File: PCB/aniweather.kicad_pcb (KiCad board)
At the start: 2 copper layers, 55 x 75 mm, 36 parts, among them SW2 SW_Push, SW3 SW_Push, SW4 SW_DIP_x01, U4 TPS2116DRL, U5 TPS63001

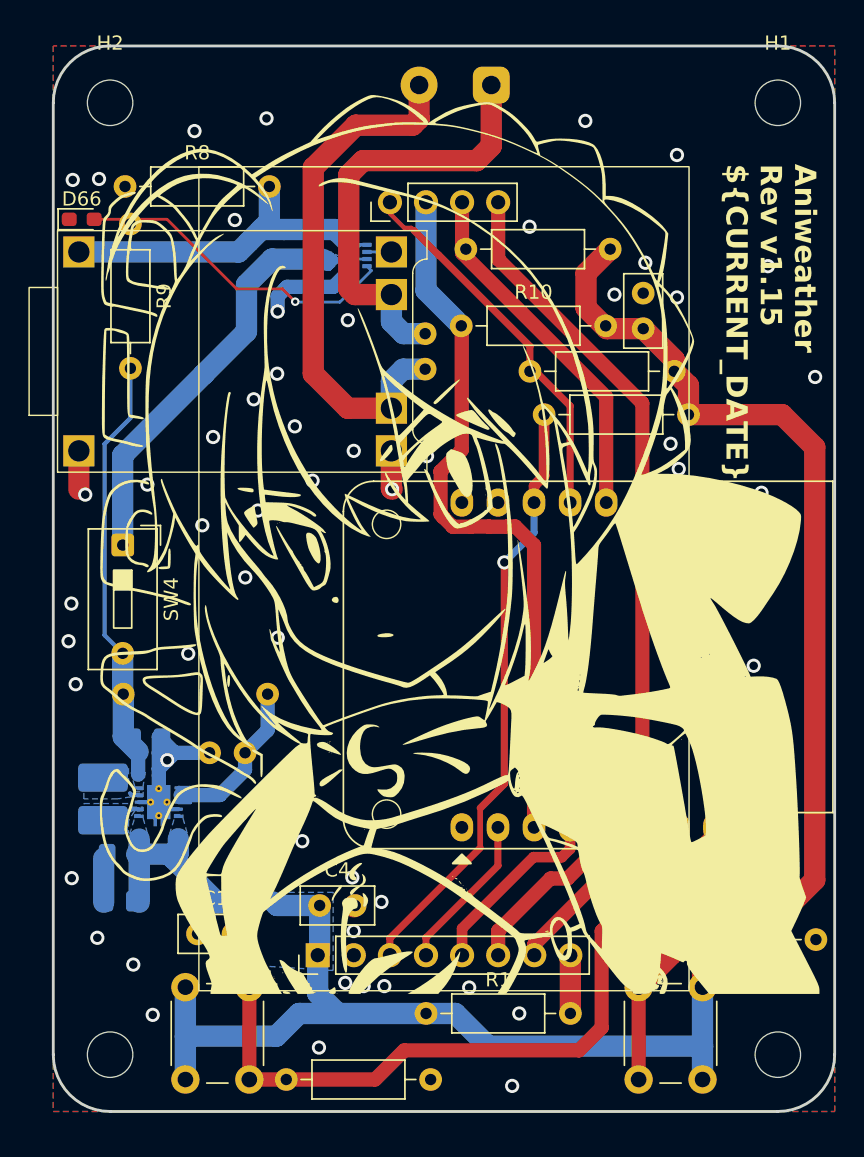
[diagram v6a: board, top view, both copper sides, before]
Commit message: Use SMD resistors
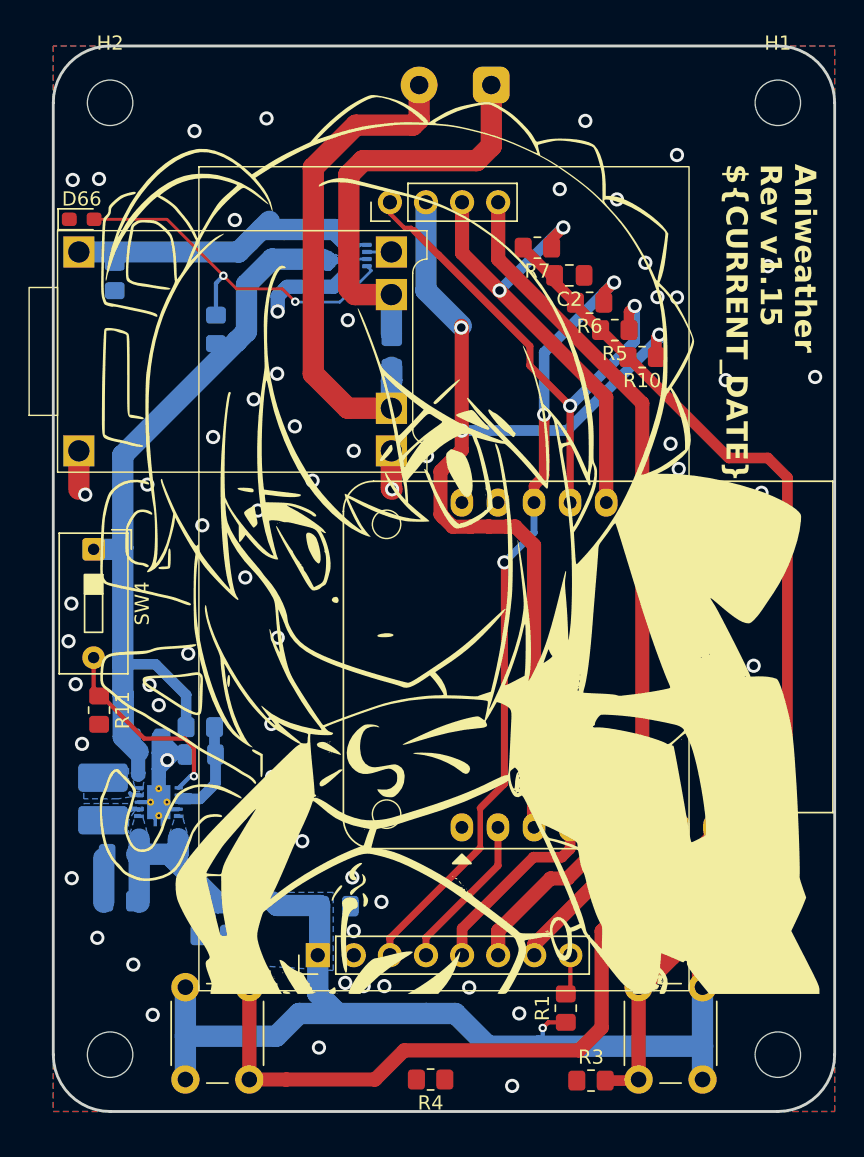
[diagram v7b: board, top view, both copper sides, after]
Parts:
- added R11: 4.7k, Resistor_SMD:R_0805_2012Metric_Pad1.20x1.40mm_HandSolder, F.Cu at (115.9, 110.2)
- C1, C4: footprint Capacitor_THT:C_Disc_D5.0mm_W2.5mm_P2.50mm -> Capacitor_SMD:C_0805_2012Metric_Pad1.18x1.45mm_HandSolder; moved to B.Cu
- C2, C3, C5, C9: footprint Capacitor_THT:C_Disc_D5.0mm_W2.5mm_P2.50mm -> Capacitor_SMD:C_0805_2012Metric_Pad1.18x1.45mm_HandSolder
- R1, R10, R2, R3, R4, R5, R6, R7: footprint Resistor_THT:R_Axial_DIN0207_L6.3mm_D2.5mm_P10.16mm_Horizontal -> Resistor_SMD:R_0805_2012Metric_Pad1.20x1.40mm_HandSolder
- R8, R9: footprint Resistor_THT:R_Axial_DIN0207_L6.3mm_D2.5mm_P10.16mm_Horizontal -> Resistor_SMD:R_0805_2012Metric_Pad1.20x1.40mm_HandSolder; moved to B.Cu
- moved R3 18.7 mm to (150.6, 136.2), turned to 0 degrees
- moved R10 12.9 mm to (154.2, 85.3), turned to 180 degrees
- moved R1 9.84 mm to (148.8, 131.2), turned to 90 degrees
- moved R9 9.55 mm to (124.2, 83.4)
- moved R6 8.50 mm to (150.4, 81.5), turned to 180 degrees
- moved R5 6.64 mm to (152.2, 83.4), turned to 180 degrees
- moved R8 6.38 mm to (117.0, 79.7), turned to 90 degrees
- moved C2 5.35 mm to (149.0, 79.6), turned to 180 degrees
- moved R2 5.28 mm to (123.0, 111.4)
- moved R7 5.04 mm to (146.8, 77.6), turned to 180 degrees
- moved C5 3.13 mm to (123.1, 113.3)
- moved C3 2.70 mm to (136.5, 85.0)
- moved SW4 2.07 mm to (115.5, 98.9)
- moved C1 1.13 mm to (124.0, 126.0)
- moved C4 1.13 mm to (132.6, 124.0)
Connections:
- C5 pad 1: Net-(U5-EN) -> Net-(U5-PS/SYNC)
- R2 pad 1: Net-(U5-EN) -> Net-(U5-PS/SYNC)
- SW4 pad 1: Net-(SW4-Pad1) -> +5V
- SW4 pad 2: +5V -> Net-(U5-EN)
- U4 pad 2: Net-(SW4-Pad1) -> +5V
- U4 pad 7: Net-(SW4-Pad1) -> +5V
- U5 pad 7: Net-(U5-EN) -> Net-(U5-PS/SYNC)
- U5 pad 8: Net-(U5-EN) -> Net-(U5-PS/SYNC)
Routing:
- net Net-(SW4-Pad1): track 34.6 -> 0.00 mm
- net +5V: track 30.3 -> 61.0 mm
- net MOSI: track 68.8 -> 87.5 mm, vias 0 -> 3
- net CS_LCD: track 42.5 -> 55.6 mm, vias 1 -> 3
- net SD_CS: track 26.9 -> 37.5 mm, vias 0 -> 2
- net Net-(U5-PS/SYNC): track 0.00 -> 9.50 mm
- net +3.3V: track 155.0 -> 146.6 mm, vias 0 -> 2
- net MISO: track 25.3 -> 33.4 mm, vias 0 -> 2
- net Net-(U5-EN): track 17.8 -> 14.4 mm, vias 0 -> 1
- net Net-(D66-A): track 23.3 -> 26.3 mm, vias 1 -> 2
- net GND: track 29.1 -> 26.5 mm, vias 65 -> 74
- net VIN+: track 28.7 -> 26.3 mm
- net Net-(U2-A5): track 18.9 -> 21.3 mm
- net Net-(BT1-+): track 31.4 -> 29.5 mm
- net Net-(BT1--): track 36.9 -> 35.2 mm
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- removed copper zone on B.Cu, net Net-(SW4-Pad1)

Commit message: Final revision
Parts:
- moved R4 2.31 mm to (136.9, 136.2)
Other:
- board text removed: "${TITLE} Rev ${REVISION} ${CURRENT_DATE}"
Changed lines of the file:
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@@
 		(title "Aniweather")
 		(date "2024-12-06")
-		(rev "v1.15")
+		(rev "v1.16")
 		(company "Cyao")
 		(comment 1 "Anime weather station")
@@
 			(at 0 -1.65 0)
 			(layer "F.SilkS")
+			(hide yes)
 			(effects
 				(font
@@
 			(at 0 -1.65 0)
 			(layer "F.SilkS")
+			(hide yes)
 			(effects
 				(font
@@
 			(at 0 -1.65 90)
 			(layer "F.SilkS")
+			(hide yes)
 			(effects
 				(font
@@
 			(at 0 -1.43 180)
 			(layer "F.SilkS")
+			(hide yes)
 			(effects
 				(font
@@
 			(layer "F.SilkS")
 		)
-		(fp_text user "${REFERENCE}"
-			(at 0 2.5 90)
-			(unlocked yes)
-			(layer "F.Fab")
-			(effects
-				(font
-					(size 1 1)
-					(thickness 0.15)
-				)
-			)
-		)
 		(pad "0" thru_hole rect
 			(at 4 10.5 180)
@@
 			(at 0 -1.68 0)
 			(layer "F.SilkS")
+			(hide yes)
 			(effects
 				(font
@@
 			(at 0 -1.65 0)
 			(layer "F.SilkS")
+			(hide yes)
 			(effects
 				(font
@@
 	(footprint "Resistor_SMD:R_0805_2012Metric_Pad1.20x1.40mm_HandSolder"
 		(layer "F.Cu")
-		(at 139.26 136.175 180)
+		(at 136.95 136.2 180)
 		(descr "Resistor SMD 0805 (2012 Metric), square (rectangular) end terminal, IPC_7351 nominal with elongated pad for handsoldering. (Body size source: IPC-SM-782 page 72, https://www.pcb-3d.com/wordpress/wp-content/uploads/ipc-sm-782a_amendment_1_and_2.pdf), generated with kicad-footprint-generator")
 		(tags "resistor handsolder")
@@
 			(at 3.81 -3.42 90)
 			(layer "F.SilkS")
+			(hide yes)
 			(effects
 				(font
@@
 			(at 0 -4.2 0)
 			(layer "F.SilkS")
+			(hide yes)
 			(effects
 				(font
@@
 			(at 0 -1.65 0)
 			(layer "F.SilkS")
+			(hide yes)
 			(effects
 				(font
@@
 			(at 0 1.68 90)
 			(layer "B.SilkS")
+			(hide yes)
 			(effects
 				(font
@@
 		(attr smd)
 		(fp_line
-			(start -0.261252 0.735)
-			(end 0.261252 0.735)
-			(stroke
-				(width 0.12)
-				(type solid)
-			)
-			(layer "B.SilkS")
-		)
-		(fp_line
-			(start -0.261252 -0.735)
-			(end 0.261252 -0.735)
-			(stroke
-				(width 0.12)
-				(type solid)
-			)
-			(layer "B.SilkS")
-		)
-		(fp_line
 			(start -1.88 0.98)
 			(end 1.88 0.98)
@@
 			(unlocked yes)
 			(layer "B.SilkS")
+			(hide yes)
 			(effects
 				(font
@@
 		(attr exclude_from_pos_files)
 		(fp_line
-			(start 6.6 -1.5)
-			(end 6.6 1.5)
-			(stroke
-				(width 0.12)
-				(type solid)
-			)
-			(layer "B.SilkS")
-		)
-		(fp_line
-			(start 6.6 -1.5)
-			(end -1.5 -1.5)
-			(stroke
-				(width 0.12)
-				(type solid)
-			)
-			(layer "B.SilkS")
-		)
-		(fp_line
-			(start -1.5 1.5)
-			(end 6.6 1.5)
-			(stroke
-				(width 0.12)
-				(type solid)
-			)
-			(layer "B.SilkS")
-		)
-		(fp_line
-			(start -1.5 1.5)
-			(end -1.5 -1.5)
-			(stroke
-				(width 0.12)
-				(type solid)
-			)
-			(layer "B.SilkS")
-		)
-		(fp_line
 			(start 6.88 -1.8)
 			(end 6.88 1.8)
@@
 			(at 2.875 0.375 90)
 			(layer "B.SilkS")
+			(hide yes)
 			(effects
 				(font
@@
 			(unlocked yes)
 			(layer "B.SilkS")
+			(hide yes)
 			(effects
 				(font
@@
 		(sheetfile "aniweather.kicad_sch")
 		(attr smd)
-		(fp_line
-			(start 0.65 -1.16)
-			(end -0.65 -1.16)
-			(stroke
-				(width 0.12)
-				(type default)
-			)
-			(layer "B.SilkS")
-		)
-		(fp_line
-			(start 0.65 1.16)
-			(end -0.4 1.16)
-			(stroke
-				(width 0.12)
-				(type default)
-			)
-			(layer "B.SilkS")
-		)
 		(fp_poly
 			(pts
@@
 			(at 0 1.65 90)
 			(layer "B.SilkS")
+			(hide yes)
 			(effects
 				(font
@@
 			(at 0 1.68 180)
 			(layer "B.SilkS")
+			(hide yes)
 			(effects
 				(font
@@
 			(at 0 1.65 90)
 			(layer "B.SilkS")
+			(hide yes)
 			(effects
 				(font
@@
 			(at 0 1.68 180)
 			(layer "B.SilkS")
+			(hide yes)
 			(effects
 				(font
@@
 			(at 0 1.68 0)
 			(layer "B.SilkS")
+			(hide yes)
 			(effects
 				(font
@@
 		(attr smd)
 		(fp_line
-			(start -0.261252 0.735)
-			(end 0.261252 0.735)
-			(stroke
-				(width 0.12)
-				(type solid)
-			)
-			(layer "B.SilkS")
-		)
-		(fp_line
-			(start -0.261252 -0.735)
-			(end 0.261252 -0.735)
-			(stroke
-				(width 0.12)
-				(type solid)
-			)
-			(layer "B.SilkS")
-		)
-		(fp_line
 			(start 1.88 0.98)
 			(end 1.88 -0.98)
@@
 		(layer "Edge.Cuts")
 	)
-	(gr_text "${TITLE} \nRev ${REVISION} \n${CURRENT_DATE}"
-		(at 159.9 71.725 -90)
-		(layer "F.SilkS")
-		(effects
-			(font
-				(size 1.5 1.5)
-				(thickness 0.3)
-				(bold yes)
-			)
-			(justify left bottom)
-		)
-	)
 	(dimension
